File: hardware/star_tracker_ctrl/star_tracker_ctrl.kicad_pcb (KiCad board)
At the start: 2 copper layers, 127 x 84 mm, 65 parts, among them J1 12V IN, J10 I2C EXP, J11 SPARE IO, J2 CAM USB-A, J20 ESP32 L, J21 ESP32 R, J3 CAM 5V, J30 TMC2209 L, J31 TMC2209 R, J4 MOTOR, J5 DIAG, J6 DS3231, J7 AS5600, J8 HOME, J9 GPS v2, Q1 IRF4905, Q2 IRF4905, Q3 2N3904, SW1 CONFIG, U2 LM2596T-5.0

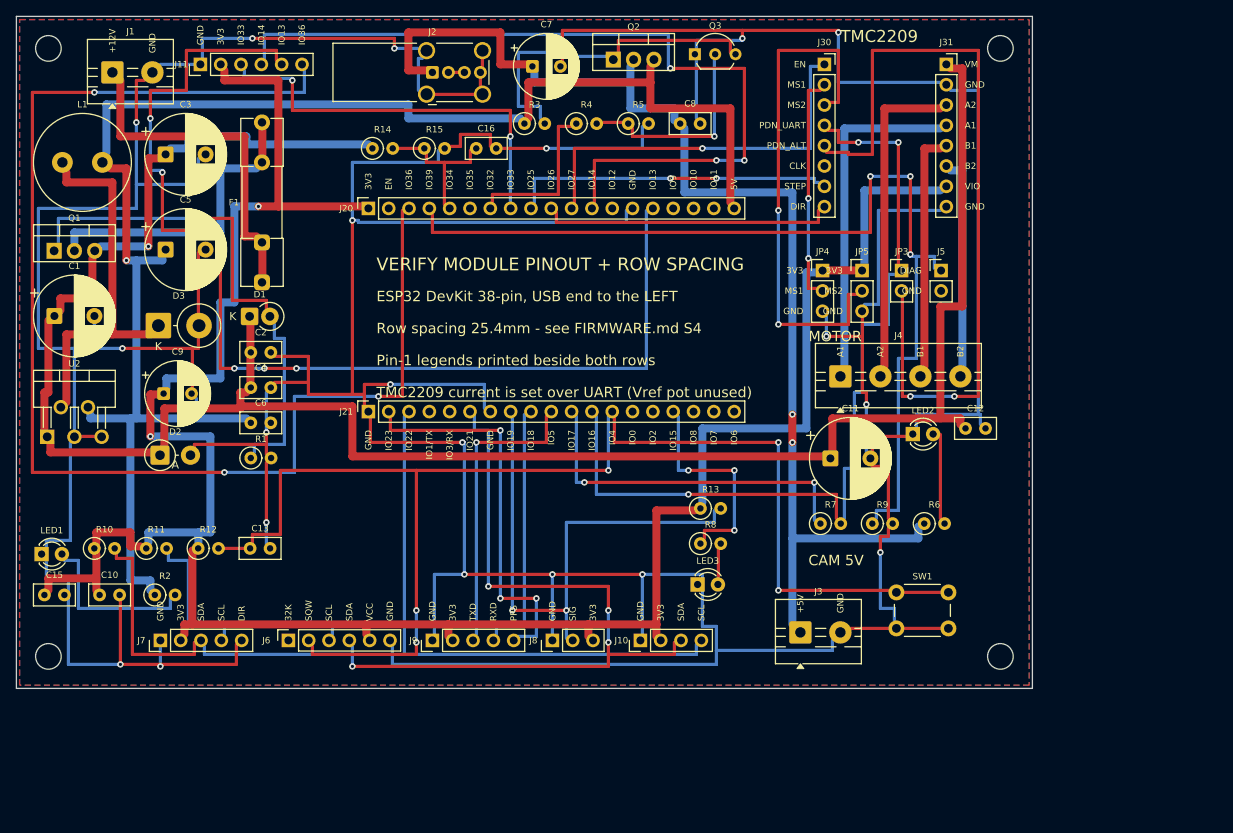
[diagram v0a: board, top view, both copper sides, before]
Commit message: Rev B: fix a mirrored ESP32 socket, add GPS, grow the board to 150x100
The important one first. The ESP32 socket in rev A was MIRRORED. The module's
left column was on the top row with pin 1 at the left, and that combination is
neither of the two legal placements -- the transform from module coordinates
to board coordinates had determinant -1, so the module would have had to be
flipped over to fit. Every pin was on the wrong signal. Fabricated, it would
have been scrap with no obvious cause.

A DevKitC laid on its side has exactly two legal orientations:

  90 CW : left column = TOP row, pin 1 at the RIGHT, USB at the LEFT
  90 CCW: left column = BOTTOM row, pin 1 at the LEFT, USB at the RIGHT

Both sockets are now at rotation 270, pin 1 at the right-hand end, USB
pointing left. The rule is written into place.py so it cannot be lost again.

Silkscreen now makes it checkable by eye, which is the real defence: dashed
body outlines for the ESP32 and the TMC2209, a large "USB <<<" at the correct
end, a bold "1" beside pin 1 of all four sockets, per-pin signal names on
every connector, and the orientation stated in words under the module.

GPS is in, as v1 rather than a v2 reservation. A GY-NEO6MV2 supplies time,
date and position; the DS3231 stays, because a GPS cannot wake a sleeping
ESP32 at a time, needs sky view and ~45 mA just to know the time, and has
nothing to say under cloud. The RTC is the bootstrap and the GPS disciplines
it: TIME_SYNC sets the RTC from GPS UTC each evening, records the drift as a
free nightly measurement of the crystal, takes lat/lon for the twilight
calculation, then powers the GPS down. gps_policy defaults to best_effort --
no fix must never cost a night.

The GPS gets a 2N3906 high-side switch off 5 V driven by a 2N3904 on GPIO 2.
Both rails stay up through deep sleep, so an unswitched module would draw
30-45 mA around the clock, roughly 5 Wh a day for a part with ninety seconds
of work each evening. Switched, it costs under 0.1 Wh a nigh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
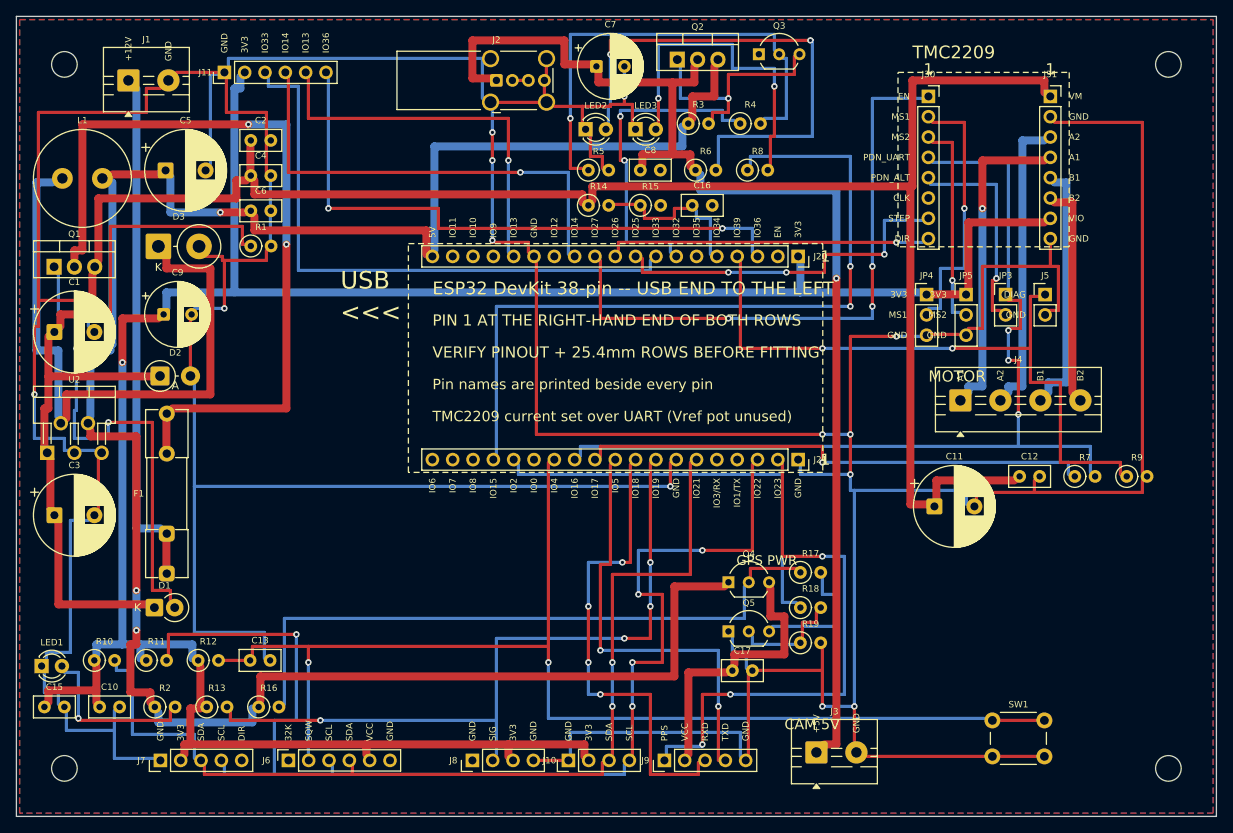
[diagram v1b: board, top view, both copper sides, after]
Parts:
- added C17: 100nF, Capacitor_THT:C_Disc_D5.0mm_W2.5mm_P2.50mm, F.Cu at (89.5, 81.8)
- added Q4: 2N3906, Package_TO_SOT_THT:TO-92_Inline_Wide, F.Cu at (89.0, 70.7)
- added Q5: 2N3904, Package_TO_SOT_THT:TO-92_Inline_Wide, F.Cu at (89.0, 76.9)
- added R16: 10k, Resistor_THT:R_Axial_DIN0207_L6.3mm_D2.5mm_P2.54mm_Vertical, F.Cu at (30.3, 86.3)
- added R17: 1k, Resistor_THT:R_Axial_DIN0207_L6.3mm_D2.5mm_P2.54mm_Vertical, F.Cu at (98.0, 69.5)
- added R18: 10k, Resistor_THT:R_Axial_DIN0207_L6.3mm_D2.5mm_P2.54mm_Vertical, F.Cu at (98.0, 73.9)
- added R19: 100k, Resistor_THT:R_Axial_DIN0207_L6.3mm_D2.5mm_P2.54mm_Vertical, F.Cu at (98.0, 78.3)
- J8: footprint Connector_PinHeader_2.54mm:PinHeader_1x03_P2.54mm_Vertical -> Connector_PinHeader_2.54mm:PinHeader_1x04_P2.54mm_Vertical
- J9: value GPS v2 -> GPS
- moved R13 66.5 mm to (23.8, 86.3)
- moved LED3 57.4 mm to (77.4, 14.1)
- moved LED2 55.9 mm to (71.2, 14.1)
- moved J20 54.1 mm to (97.7, 30.0), turned to -90 degrees
- moved J21 54.1 mm to (97.7, 55.4), turned to -90 degrees
- moved R6 52.6 mm to (84.9, 19.2)
- moved C3 47.2 mm to (4.75, 62.4)
- moved R8 47.0 mm to (91.4, 19.2)
- moved D1 38.3 mm to (17.2, 73.9)
- moved F1 38.3 mm to (18.8, 69.7)
- moved J9 32.6 mm to (81.0, 93.0)
- moved R7 32.3 mm to (132.3, 57.5)
- moved R9 32.3 mm to (138.8, 57.5)
- moved C16 27.9 mm to (84.5, 23.6)
- moved R14 27.9 mm to (71.5, 23.6)
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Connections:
- J21 pad 15: (no net) -> GPS_EN
- J9 pad 1: GND -> PPS
- J9 pad 2: +3V3 -> GPS_VCC
- J9 pad 3: GPS_TX -> GPS_RX
- J9 pad 4: GPS_RX -> GPS_TX
- J9 pad 5: PPS -> GND
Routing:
- net SPARE13: track 138.5 -> 46.8 mm, vias 5 -> 1
- net SPARE36: track 163.2 -> 74.8 mm, vias 3 -> 2
- net GPS_B: track 0.00 -> 79.0 mm
- net +5V: track 188.5 -> 263.5 mm, vias 1 -> 3
- net PDN_ALT: track 97.5 -> 25.5 mm, vias 2 -> 1
- net LED_ST: track 26.0 -> 95.0 mm, vias 3 -> 2
- net +12V_F: track 35.0 -> 96.2 mm, vias 0 -> 2
- net LED2_A: track 10.5 -> 63.0 mm, vias 0 -> 2
- net GPS_EN: track 0.00 -> 52.0 mm
- net SPARE14: track 102.8 -> 57.0 mm, vias 3 -> 1
- net GND: track 777.8 -> 732.5 mm, vias 20 -> 14
- net SCL: track 108.0 -> 149.2 mm, vias 0 -> 5
- net TMC_DIAG: track 121.2 -> 81.5 mm, vias 3 -> 2
- net MS2: track 62.8 -> 24.8 mm, vias 2 -> 1
- net GATE_RP: track 61.5 -> 98.0 mm, vias 1 -> 2
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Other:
- board size 127 x 84 mm -> 150 x 100 mm
- board text added: "1"
- board text added: "<<<"
- board text added: "ESP32 DevKit 38-pin -- USB END TO THE LEFT"
- board text added: "GPS PWR"
- board text added: "PIN 1 AT THE RIGHT-HAND END OF BOTH ROWS"
- board text added: "Pin names are printed beside every pin"
- board text added: "TMC2209 current set over UART (Vref pot unused)"
- board text added: "USB"
- board text added: "VERIFY PINOUT + 25.4mm ROWS BEFORE FITTING"
- board text removed: "ESP32 DevKit 38-pin, USB end to the LEFT"
- board text removed: "Pin-1 legends printed beside both rows"
- board text removed: "Row spacing 25.4mm - see FIRMWARE.md S4"
- board text removed: "TMC2209 current is set over UART (Vref pot unused)"
- board text removed: "VERIFY MODULE PINOUT + ROW SPACING"

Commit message: Controller board Rev C for the 30-pin ideaspark ESP32
Pin check (firmware/pincheck, 2026-09-27): ESP32-D0WD-V3, 4 MB, no PSRAM;
the on-board OLED answers at 0x3C on GPIO 21/22, so it shares the sensor
bus and GPIO 4 stays free for WAKE.

design.py: the 30-pin map (15 per side, rows 27.94 mm). Upper row serves
the driver, camera switch, divider and status LED; lower row the bottom
connector strip. Changes from Rev B: TMC UART 33/14, DIAG 36, LED_ST 13,
GPS_EN 17 (GPIO 2 left free for download mode), J11 now 4 pins (39, 35).
GPS UART nets named by direction. REV = "C".

route.py: vias keep the fab's hole-to-hole minimum from every pad and via
whatever the net (a GND via sat 0.19 mm from a GND pad's hole); the GND
stitch runs twice; GND_RESCUE pads get an escape before any signal is
routed -- the bottom strip's four GND end pins, which signal tracks fenced
in on both layers.

Result: fully routed, ERC 0, DRC 0 unconnected / clearance / hole-to-hole;
only cosmetic silkscreen overlaps. Board render and schematic PDF
regenerated. FIRMWARE.md, PCB.md, HARDWARE.md, RESUME.md and README follow;
the assembly guide, its Fritzing views and PDF are rebuilt from the new
layout. KiCad lock files ignored.

Co-Authored-By: Claude Opus 5.5 <noreply@anthropic.com>
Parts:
- J11: footprint Connector_PinHeader_2.54mm:PinHeader_1x06_P2.54mm_Vertical -> Connector_PinHeader_2.54mm:PinHeader_1x04_P2.54mm_Vertical
- J20, J21: footprint Connector_PinSocket_2.54mm:PinSocket_1x19_P2.54mm_Vertical -> Connector_PinSocket_2.54mm:PinSocket_1x15_P2.54mm_Vertical
- moved J21 10.5 mm to (87.6, 57.9)
- moved J20 10.2 mm to (87.6, 30.0)
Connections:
- J11 pad 3: SPARE33 -> SPARE39
- J11 pad 4: SPARE14 -> SPARE35
- J20 pad 1: +3V3 -> (no net)
- J20 pad 10: MOT_DIR -> TMC_EN
- J20 pad 11: TMC_EN -> TMC_UART
- J20 pad 12: SPARE14 -> (no net)
- J20 pad 13: (no net) -> LED_ST
- J20 pad 15: SPARE13 -> +5V
- J20 pad 2: (no net) -> TMC_DIAG
- J20 pad 3: SPARE36 -> SPARE39
- J20 pad 4: TMC_DIAG -> VBAT_SENSE
- J20 pad 5: VBAT_SENSE -> SPARE35
- J20 pad 6: (no net) -> CAM_EN
- J20 pad 7: CAM_EN -> ESP_TX
- J20 pad 8: SPARE33 -> STEP
- J20 pad 9: STEP -> MOT_DIR
- J21 pad 1: GND -> PPS
- J21 pad 10: GPS_TX -> (no net)
- J21 pad 11: ESP_TX -> WAKE
- J21 pad 12: TMC_UART -> (no net)
- J21 pad 13: WAKE -> (no net)
- J21 pad 14: (no net) -> GND
- J21 pad 15: GPS_EN -> +3V3
- J21 pad 2: PPS -> SCL
- J21 pad 3: SCL -> (no net)
- J21 pad 5: (no net) -> SDA
- J21 pad 6: SDA -> HOME
- J21 pad 7: GND -> GPS_TX_ESP_RX
- J21 pad 8: HOME -> ESP_TX_GPS_RX
- J21 pad 9: GPS_RX -> GPS_EN
- J9 pad 3: GPS_RX -> ESP_TX_GPS_RX
- J9 pad 4: GPS_TX -> GPS_TX_ESP_RX
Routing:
- net GPS_TX_ESP_RX: track 0.00 -> 76.2 mm, vias 0 -> 3
- net SPARE36: track 74.8 -> 0.00 mm, vias 2 -> 0
- net Q3_B: track 56.5 -> 130.0 mm, vias 1 -> 6
- net SPARE33: track 73.0 -> 0.00 mm
- net SPARE39: track 0.00 -> 72.0 mm, vias 0 -> 2
- net +12V_F: track 96.2 -> 30.5 mm, vias 2 -> 0
- net SPARE35: track 0.00 -> 64.5 mm, vias 0 -> 1
- net GPS_RX: track 59.2 -> 0.00 mm, vias 4 -> 0
- net WAKE: track 145.0 -> 203.8 mm, vias 2 -> 3
- net SPARE14: track 57.0 -> 0.00 mm, vias 1 -> 0
- net GPS_TX: track 53.0 -> 0.00 mm, vias 2 -> 0
- net ESP_TX_GPS_RX: track 0.00 -> 49.2 mm, vias 0 -> 2
- net SPARE13: track 46.8 -> 0.00 mm, vias 1 -> 0
- net TMC_UART: track 116.0 -> 154.5 mm, vias 3 -> 4
- net +3V3: track 289.2 -> 320.2 mm, vias 1 -> 0
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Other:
- board text added: "ESP32 30-pin + OLED -- USB END TO THE LEFT"
- board text added: "PIN 1 (EN / IO23) AT THE RIGHT-HAND END"
- board text added: "ROWS 27.94 mm APART -- CHECK BEFORE FITTING"
- board text added: "RX0"
- board text added: "TMC2209 current set over UART"
- board text added: "TX0"
- board text added: "VIN"
- board text removed: "5V"
- board text removed: "ESP32 DevKit 38-pin -- USB END TO THE LEFT"
- board text removed: "IO0"
- board text removed: "IO1/TX"
- board text removed: "IO10"
- board text removed: "IO11"
- board text removed: "IO3/RX"
- board text removed: "IO6"
- board text removed: "IO7"
- board text removed: "IO8"
- board text removed: "IO9"
- board text removed: "PIN 1 AT THE RIGHT-HAND END OF BOTH ROWS"
- board text removed: "TMC2209 current set over UART (Vref pot unused)"
- board text removed: "VERIFY PINOUT + 25.4mm ROWS BEFORE FITTING"
